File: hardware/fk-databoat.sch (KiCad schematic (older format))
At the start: 20 parts, among them J1 CONN_01X02, J2 CONN_01X02, P1 CONN_01X03, P2 CONN_01X03, P3 CONN_01X03, P4 CONN_01X03, P5 CONN_01X03, P6 CONN_01X03, U1 VISO, U10 SERIAL_PORT_EXPANDER_4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

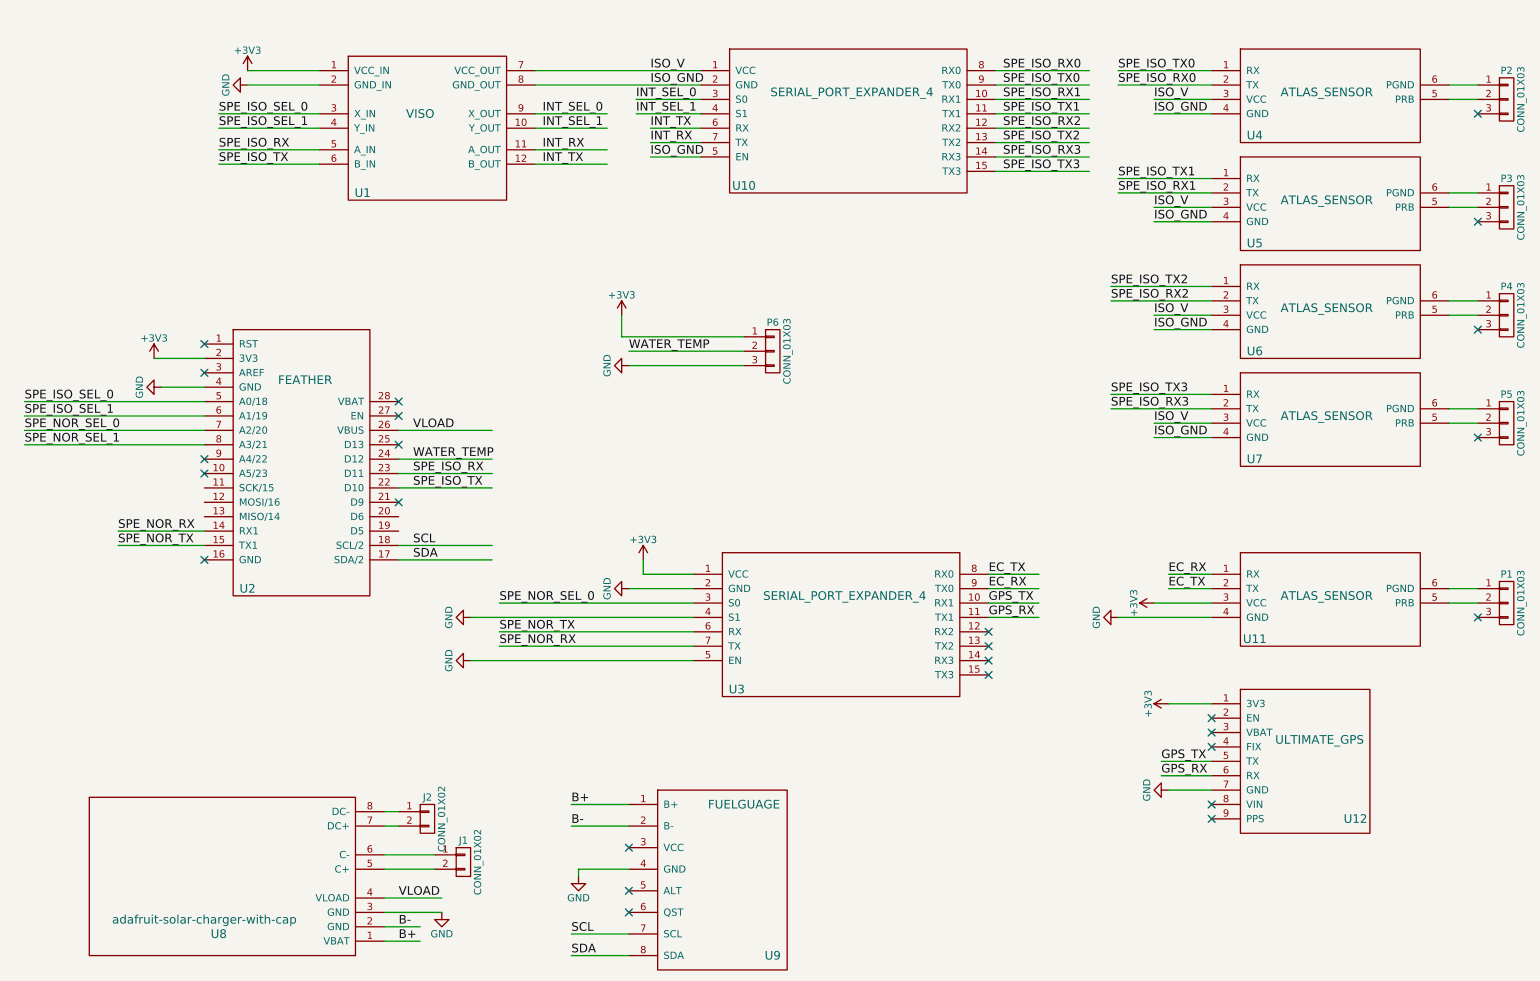
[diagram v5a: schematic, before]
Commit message: Integrate serial port expander into data boat PCB.
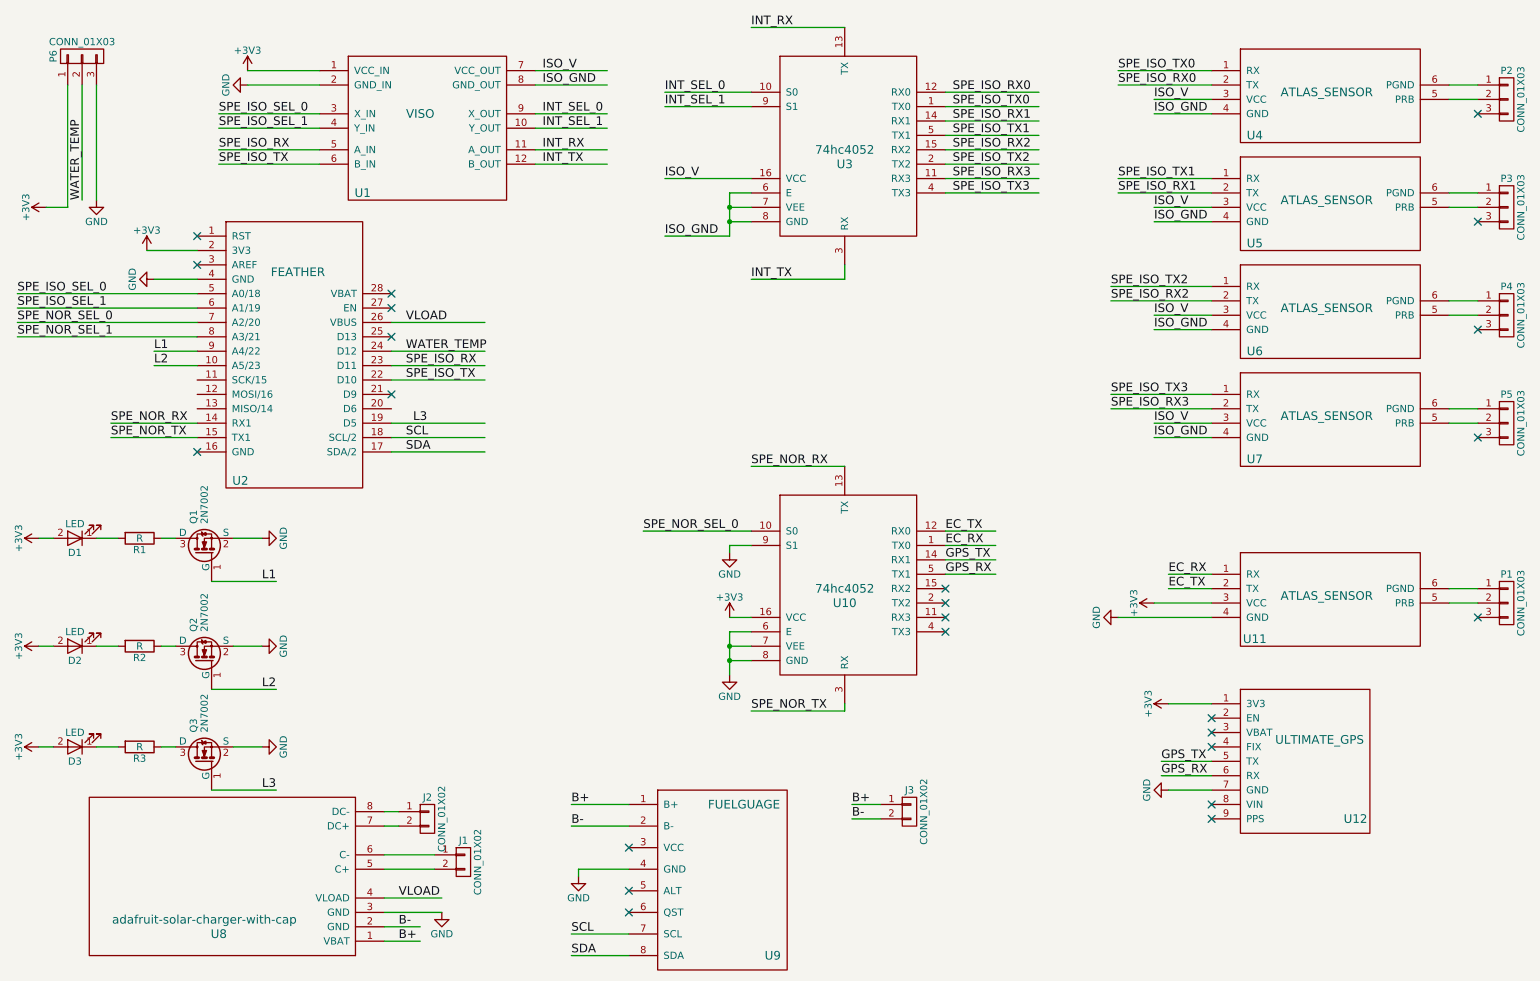
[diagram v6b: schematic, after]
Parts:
- removed U10, U3: SERIAL_PORT_EXPANDER_4, conservify:serial_port_expander_small, symbol SERIAL_PORT_EXPANDER_4
- added D1, D2, D3: LED, Resistors_SMD:R_0603_HandSoldering, symbol LED
- added J3: CONN_01X02, Connectors_JST:JST_PH_S2B-PH-SM4-TB_02x2.00mm_Angled, symbol CONN_01X02
- added Q1, Q2, Q3: 2N7002, TO_SOT_Packages_SMD:SOT-23, symbol 2N7002
- added R1, R2, R3: R, Resistors_SMD:R_0603_HandSoldering, symbol R
- added U10, U3: 74hc4052, Housings_SOIC:SOIC-16_3.9x9.9mm_Pitch1.27mm, symbol 74hc4052
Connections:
- net labels added: L1, L2, L3
- wire segments 103 -> 132
- no-connect marks 26 -> 24
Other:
- moved on the sheet: P6, U2
